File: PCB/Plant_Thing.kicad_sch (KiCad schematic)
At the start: 1 part, among them U1 nRF52820-QDxx

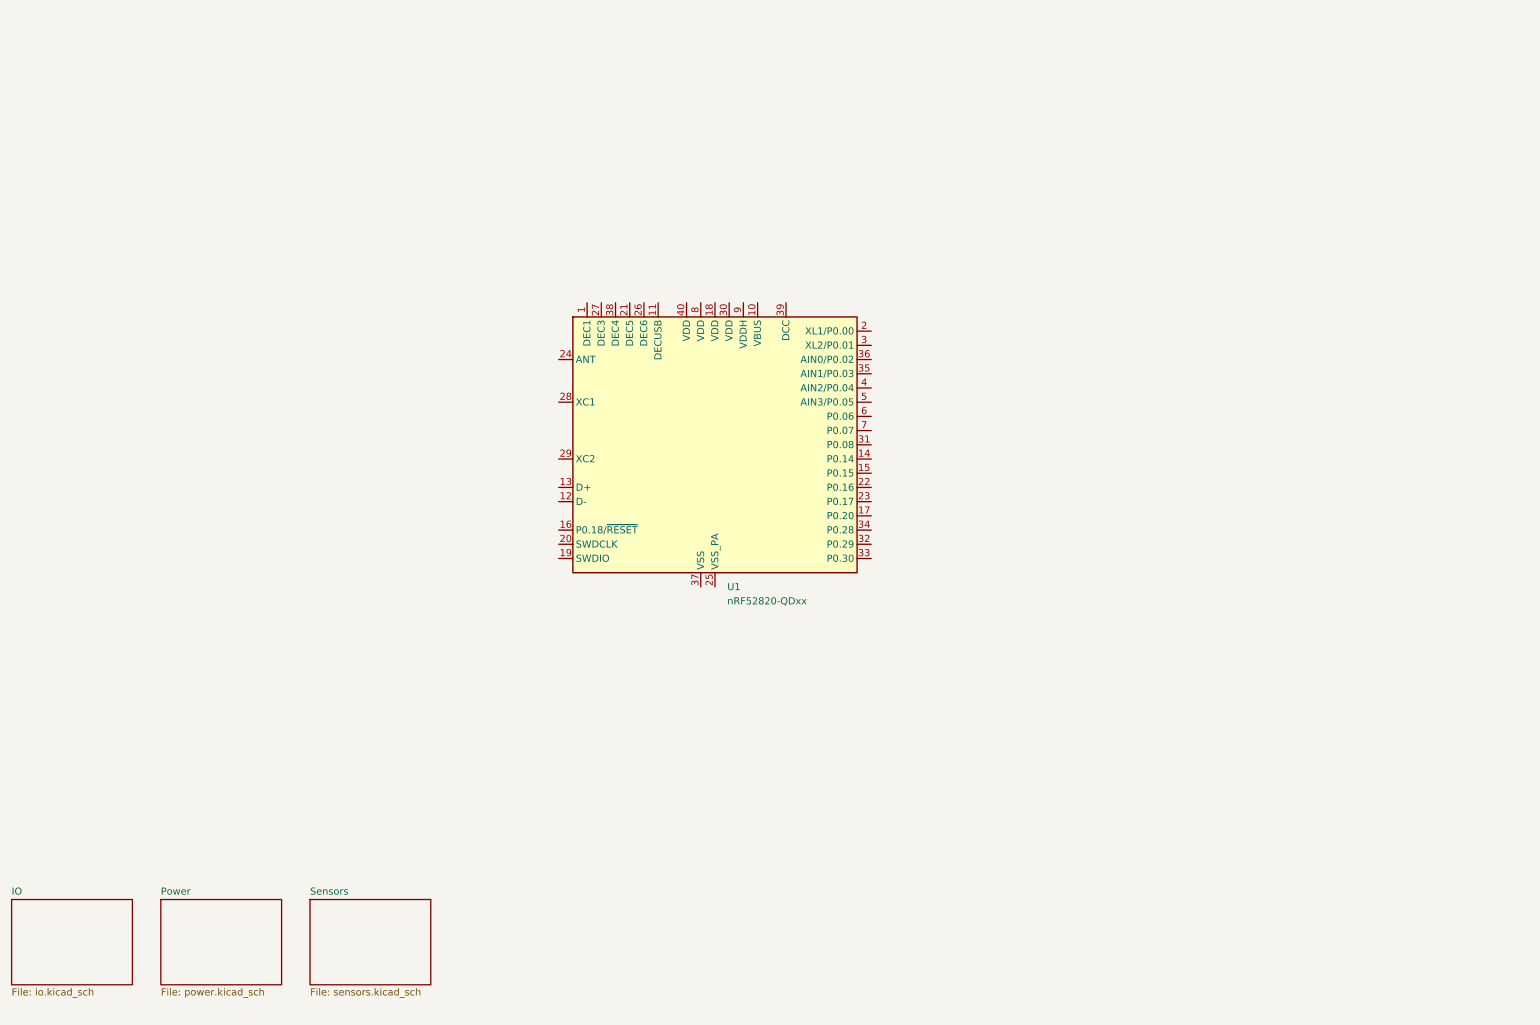
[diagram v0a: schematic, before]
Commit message: added reference schematic for nrf52820 and placed components for power
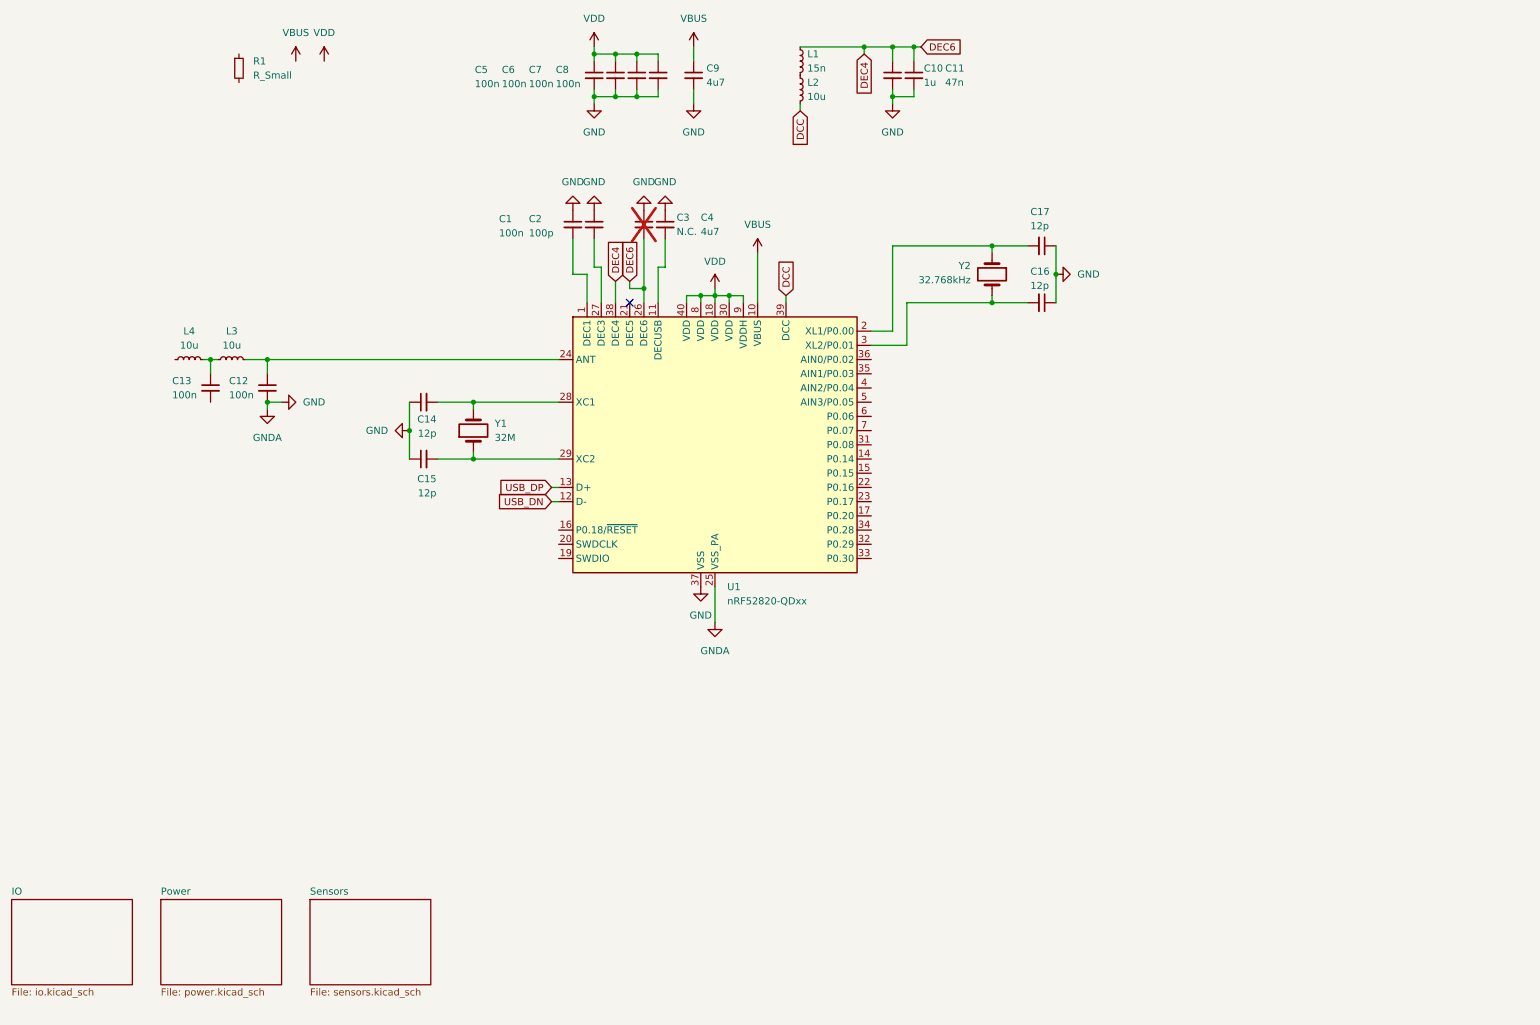
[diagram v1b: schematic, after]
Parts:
- added C1, C12, C13, C5, C6, C7, C8: 100n, symbol Device:C_Small
- added C10: 1u, symbol Device:C_Small
- added C11: 47n, symbol Device:C_Small
- added C14, C15, C16, C17: 12p, symbol Device:C_Small
- added C2: 100p, symbol Device:C_Small
- added C3: N.C., symbol Device:C_Small
- added C4, C9: 4u7, symbol Device:C_Small
- added L1: 15n, symbol Device:L_Small
- added L2, L3, L4: 10u, symbol Device:L_Small
- added R1: R_Small, symbol Device:R_Small
- added Y1: 32M, symbol Device:Crystal
- added Y2: 32.768kHz, symbol Device:Crystal
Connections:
- net at U1.1 (DEC1): now also C1.2
- net VBUS: now reaches U1.10 (VBUS)
- net VBUS: now also C9.1
- net at U1.11 (DECUSB): now also C4.2
- net USB_DN: now reaches U1.12 (D-)
- net USB_DP: now reaches U1.13 (D+)
- net VDD: now reaches U1.18 (VDD)
- net VDD: now also U1.30 (VDD), U1.40 (VDD), U1.8 (VDD), U1.9 (VDDH), C5.1, C6.1, C7.1, C8.1
- net at U1.2 (XL1/P0.00): now also C17.2, Y2.1
- net at U1.24 (ANT): now also C12.1, L3.2
- net GND: now reaches U1.25 (VSS_PA)
- net GND: now also U1.37 (VSS), U1.41 (VSS), C1.1, C10.2, C11.2, C12.2, C14.1, C15.1, C16.1, C17.1, C2.1, C3.1, C4.1, C5.2, C6.2, C7.2, C8.2, C9.2
- net DEC4: now reaches U1.26 (DEC6)
- net DEC4: now also U1.38 (DEC4), C10.1, C11.1, C3.2, L1.1
- net at U1.27 (DEC3): now also C2.2
- net at U1.28 (XC1): now also C14.2, Y1.2
- net at U1.29 (XC2): now also C15.2, Y1.1
- net at U1.3 (XL2/P0.01): now also C16.2, Y2.2
- net DCC: now reaches U1.39 (DCC)
- net DCC: now also L2.2
- new net: C13.1, L3.1, L4.2
- new net: L1.2, L2.1
- no-connect marks 0 -> 1

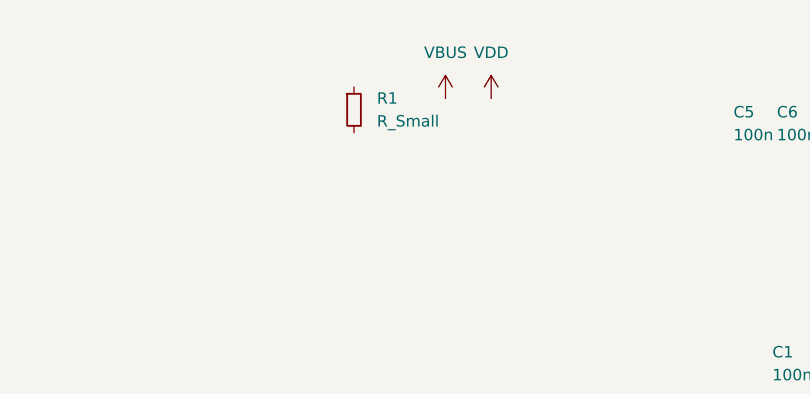
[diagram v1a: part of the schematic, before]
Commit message: Added more power components
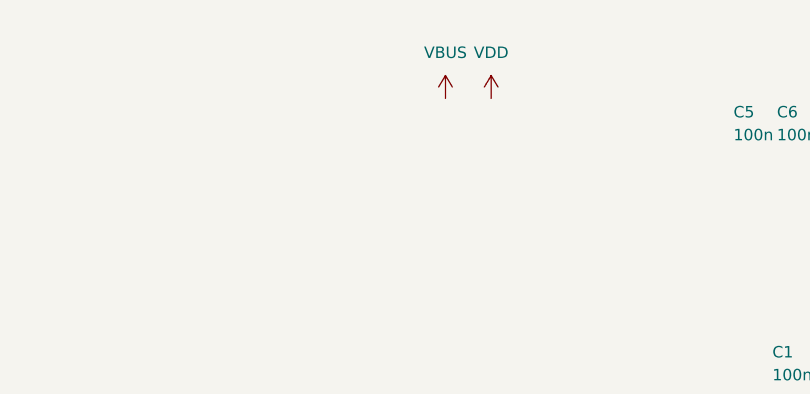
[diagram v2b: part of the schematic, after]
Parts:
- removed R1: R_Small, symbol Device:R_Small
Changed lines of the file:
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@@
-	)
-	(symbol
-		(lib_id "Device:R_Small")
-		(at 57.15 29.21 0)
-		(unit 1)
-		(exclude_from_sim no)
-		(in_bom yes)
-		(on_board yes)
-		(dnp no)
-		(fields_autoplaced yes)
-		(property "Reference" "R1"
-			(at 59.69 27.9399 0)
-			(effects
-				(font
-					(size 1.27 1.27)
-				)
-				(justify left)
-			)
-		)
-		(property "Value" "R_Small"
-			(at 59.69 30.4799 0)
-			(effects
-				(font
-					(size 1.27 1.27)
-				)
-				(justify left)
-			)
-		)
-		(property "Footprint" ""
-			(at 57.15 29.21 0)
-			(effects
-				(font
-					(size 1.27 1.27)
-				)
-				(hide yes)
-			)
-		)
-		(property "Datasheet" "~"
-			(at 57.15 29.21 0)
-			(effects
-				(font
-					(size 1.27 1.27)
-				)
-				(hide yes)
-			)
-		)
-		(property "Description" "Resistor, small symbol"
-			(at 57.15 29.21 0)
-			(effects
-				(font
-					(size 1.27 1.27)
-				)
-				(hide yes)
-			)
-		)
-		(pin "2"
-		)
-		(pin "1"
-		)
-		(instances
-			(project "Plant_Thing"
-				(path "/3604ffe7-6852-4862-a71a-75c04c0147cb"
-					(reference "R1")
-					(unit 1)
-				)
-			)
-		)
 	)
 	(symbol

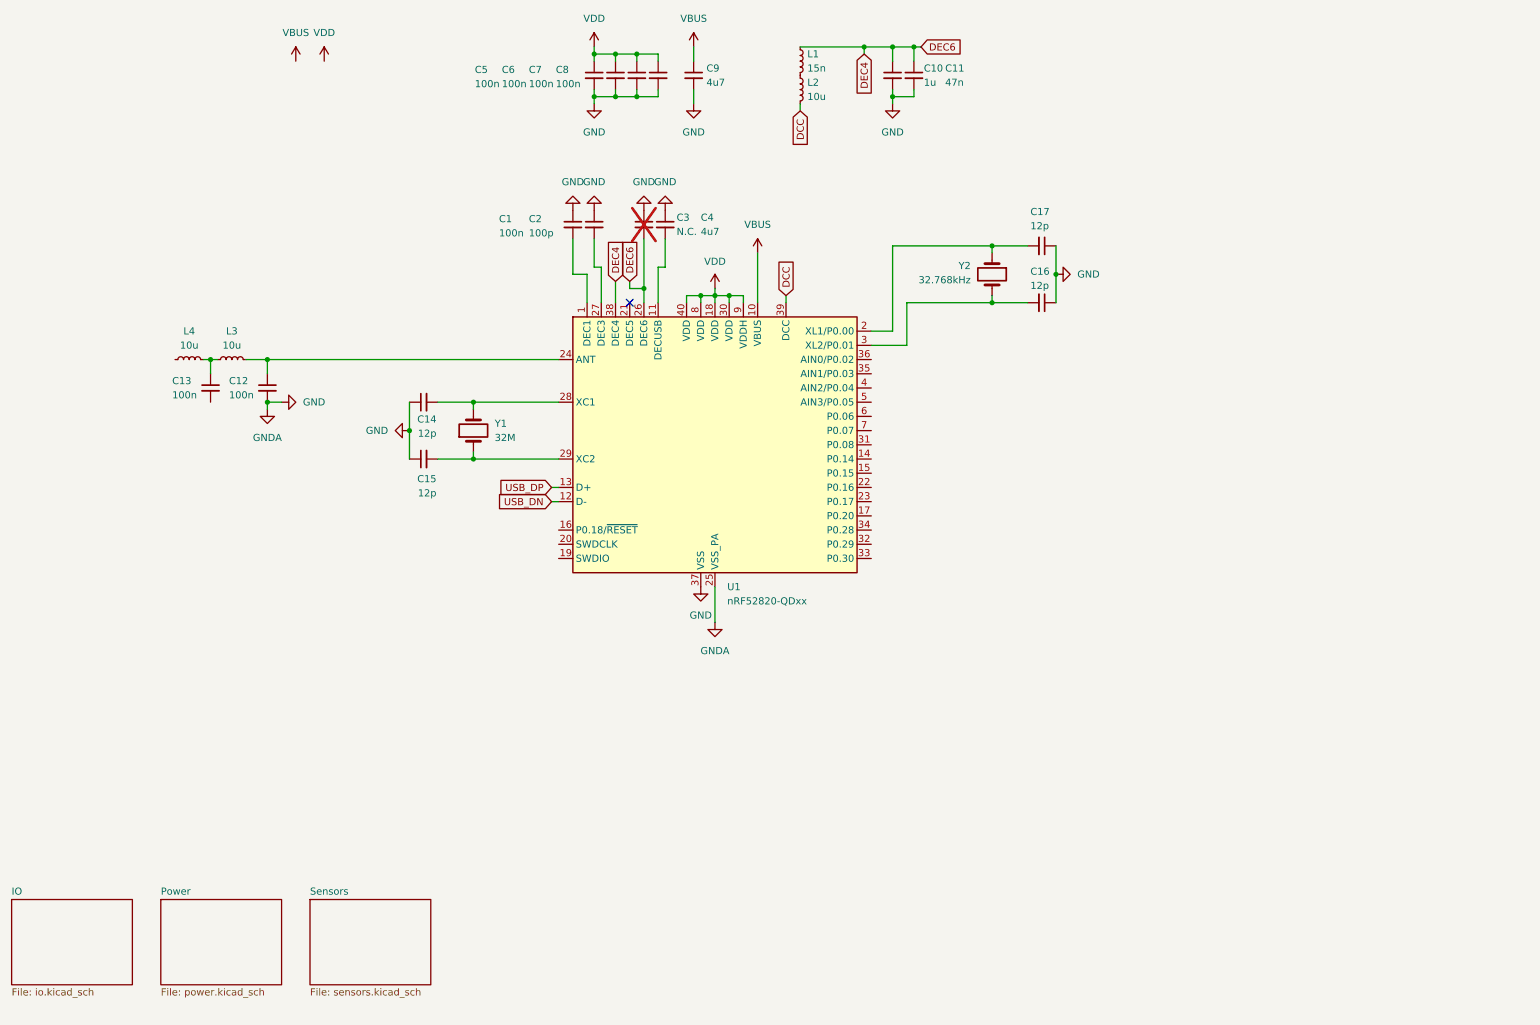
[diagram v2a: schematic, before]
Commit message: Added more components and added most needed values for the nrf example schematic
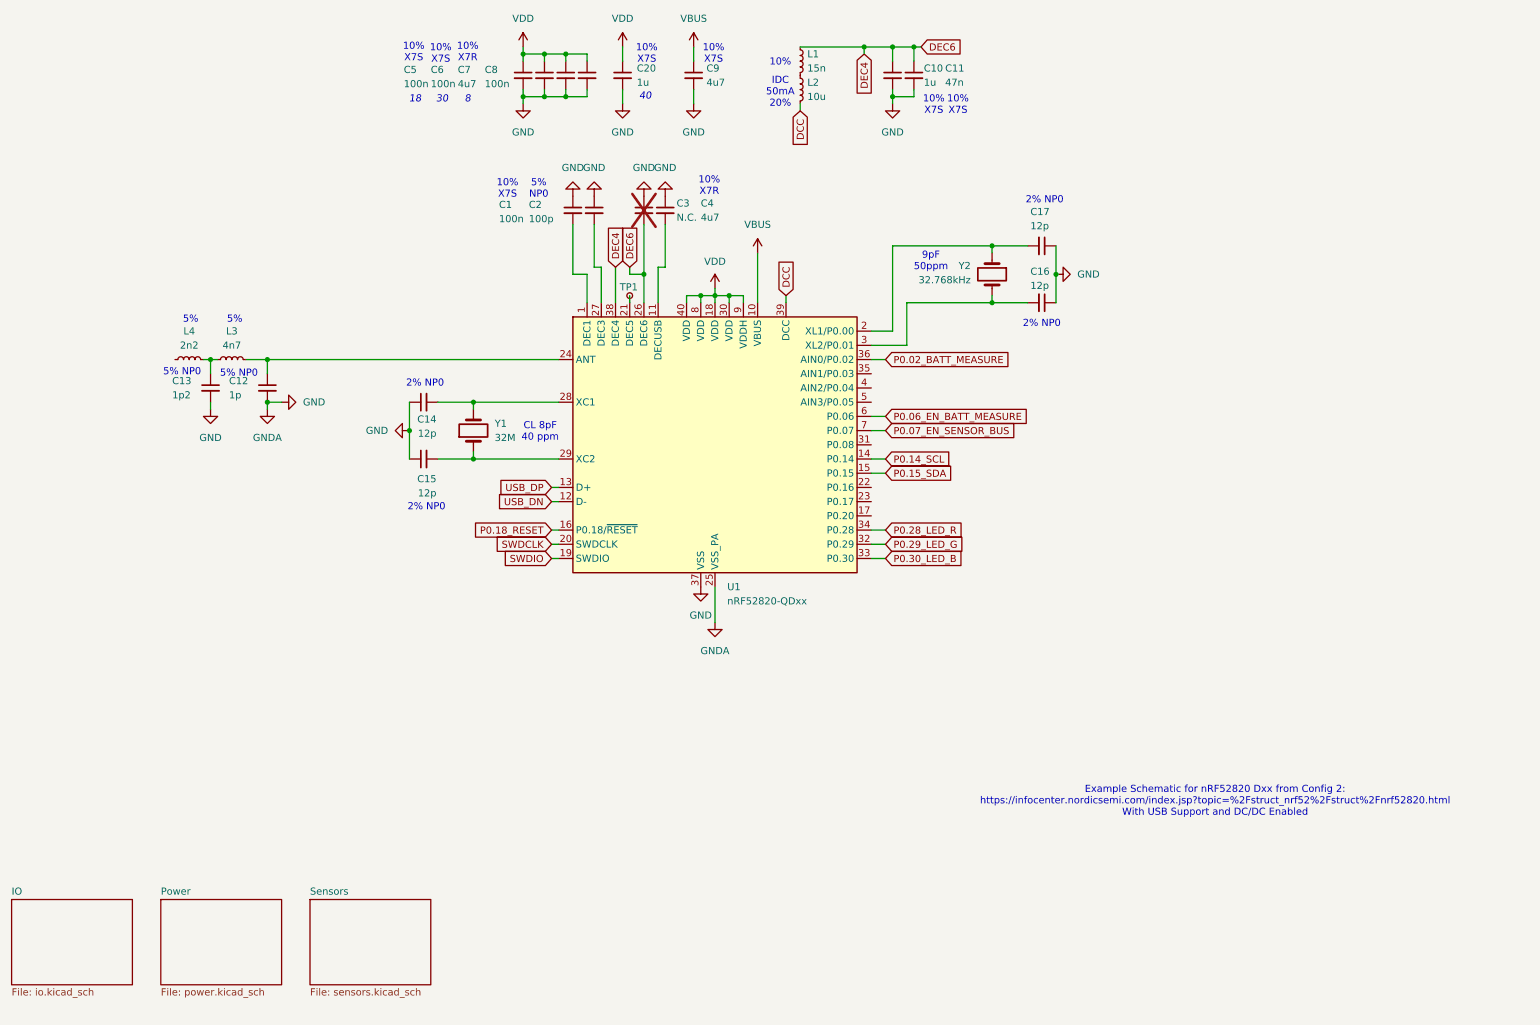
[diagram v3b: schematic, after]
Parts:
- added C20: 1u, Capacitor_SMD:C_0603_1608Metric, symbol Device:C_Small
- added TP1: TestPoint_Small, TestPoint:TestPoint_Pad_D1.0mm, symbol Connector:TestPoint_Small
- C1, C11, C14, C15, C16, C17, C2, C5, C6, C8: footprint (none) -> Capacitor_SMD:C_0402_1005Metric
- C10, C4, C9: footprint (none) -> Capacitor_SMD:C_0603_1608Metric
- C12: value 100n -> 1p; footprint (none) -> Capacitor_SMD:C_0402_1005Metric
- C13: value 100n -> 1p2; footprint (none) -> Capacitor_SMD:C_0402_1005Metric
- C7: value 100n -> 4u7; footprint (none) -> Capacitor_SMD:C_0603_1608Metric
- L1, L2: footprint (none) -> Inductor_SMD:L_0603_1608Metric
- L3: value 10u -> 4n7; footprint (none) -> Inductor_SMD:L_0402_1005Metric
- L4: value 10u -> 2n2; footprint (none) -> Inductor_SMD:L_0402_1005Metric
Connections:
- net GND: now also C13.2, C20.2
- net VDD: now also C20.1
- net P0.14_SCL: now reaches U1.14 (P0.14)
- net P0.15_SDA: now reaches U1.15 (P0.15)
- net P0.18_RESET: now reaches U1.16 (P0.18/~{RESET})
- net SWDIO: now reaches U1.19 (SWDIO)
- net SWDCLK: now reaches U1.20 (SWDCLK)
- net at U1.21 (DEC5): now also TP1.1
- net P0.29_LED_G: now reaches U1.32 (P0.29)
- net P0.30_LED_B: now reaches U1.33 (P0.30)
- net P0.28_LED_R: now reaches U1.34 (P0.28)
- net P0.02_BATT_MEASURE: now reaches U1.36 (AIN0/P0.02)
- net P0.06_EN_BATT_MEASURE: now reaches U1.6 (P0.06)
- net P0.07_EN_SENSOR_BUS: now reaches U1.7 (P0.07)
- no-connect marks 1 -> 0
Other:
- note added: "10%"
- note added: "10% X7R"
- note added: "10% X7S"
- note added: "18"
- note added: "2% NP0"
- note added: "30"
- note added: "40"
- note added: "5%"
- note added: "5% NP0"
- note added: "8"
- note added: "9pF 50ppm"
- note added: "CL 8pF 40 ppm"
- note added: "Example Schematic for nRF52820 Dxx from Config 2: https://infocenter.nordicsemi.com/index.jsp?topic=%2Fstruct_nrf52%2Fstruct%2Fnrf52820.html With USB Support and DC/DC Enabled"
- note added: "IDC 50mA 20%"
- moved on the sheet: C1, C2, C3, C4, C5, C6, C7, C8

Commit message: Added the Calathea Leaf as the outline and artwork for the project
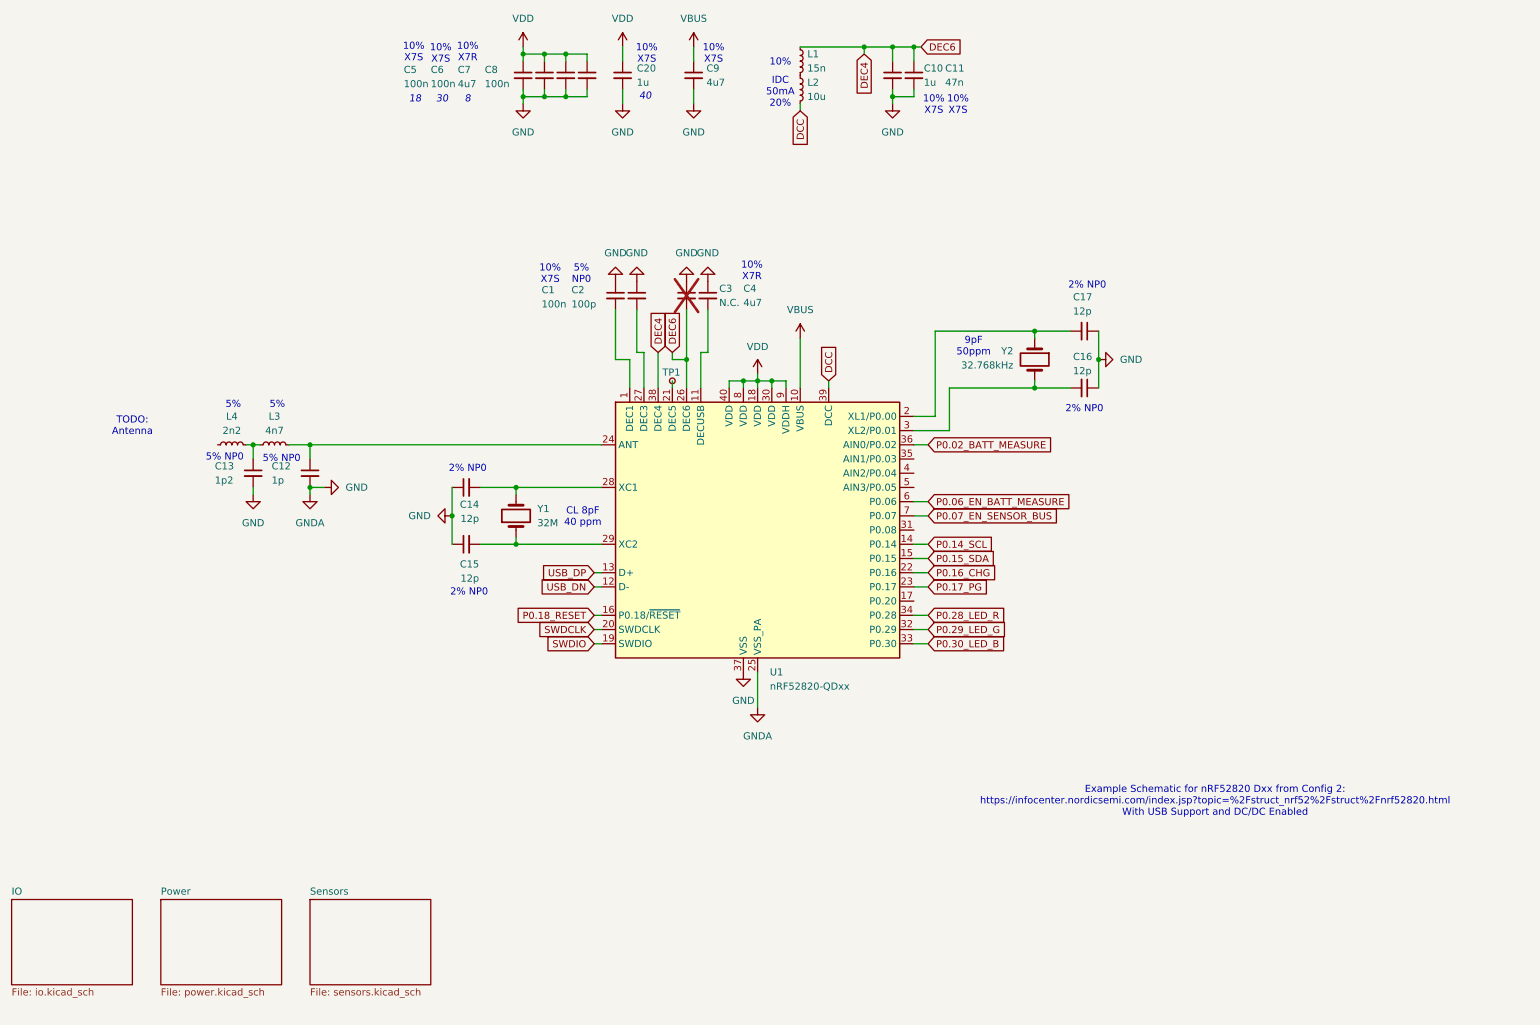
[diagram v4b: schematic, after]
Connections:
- net P0.16_CHG: now reaches U1.22 (P0.16)
- net P0.17_PG: now reaches U1.23 (P0.17)
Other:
- note added: "TODO: Antenna"
- moved on the sheet: C1, C12, C13, C14, C15, C16, C17, C2, C3, C4, L3, L4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
